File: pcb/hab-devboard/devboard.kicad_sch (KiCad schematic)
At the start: 90 parts, among them J1 S2B-PH-K-S, J2 SM04B-GHS-TB, J3 SM04B-GHS-TB, J4 2x20 Pin Header, J5 S2B-PH-K-S, Q1 DMG2301L, Q2 CSD25310Q2, Q3 BSS138, Q4 BSS138, Q5 BSS138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

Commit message: Updating pcb, adding xcode project for macOS gui
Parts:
- added H5: MountingHole, MountingHole:MountingHole_3.2mm_M3, symbol Mechanical:MountingHole
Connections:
- net 5VSNS is gone; now on net 5V_SNS: U8.1 (OUT)
- net +3V3_SBC: now also U5.4 (~{CS})
- net 5V_HEATER_EN: now also J4.18 (Pin_18)
- net 5V_PA_EN: now also J4.16 (Pin_16)
- net BATT_ALERT_N: now also J4.31 (Pin_31)
- net GPS_RST_N: now also J4.35 (Pin_35)
- net GPS_WAKE: now also J4.33 (Pin_33)
- net 5V_SNS: now reaches J4.37 (Pin_37)
- no-connect marks 41 -> 37
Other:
- note added: "CHECK THIS"
- note added: "External 5V Heater Power"
- note added: "Internal PU"
- moved on the sheet: J1, Q1, R1

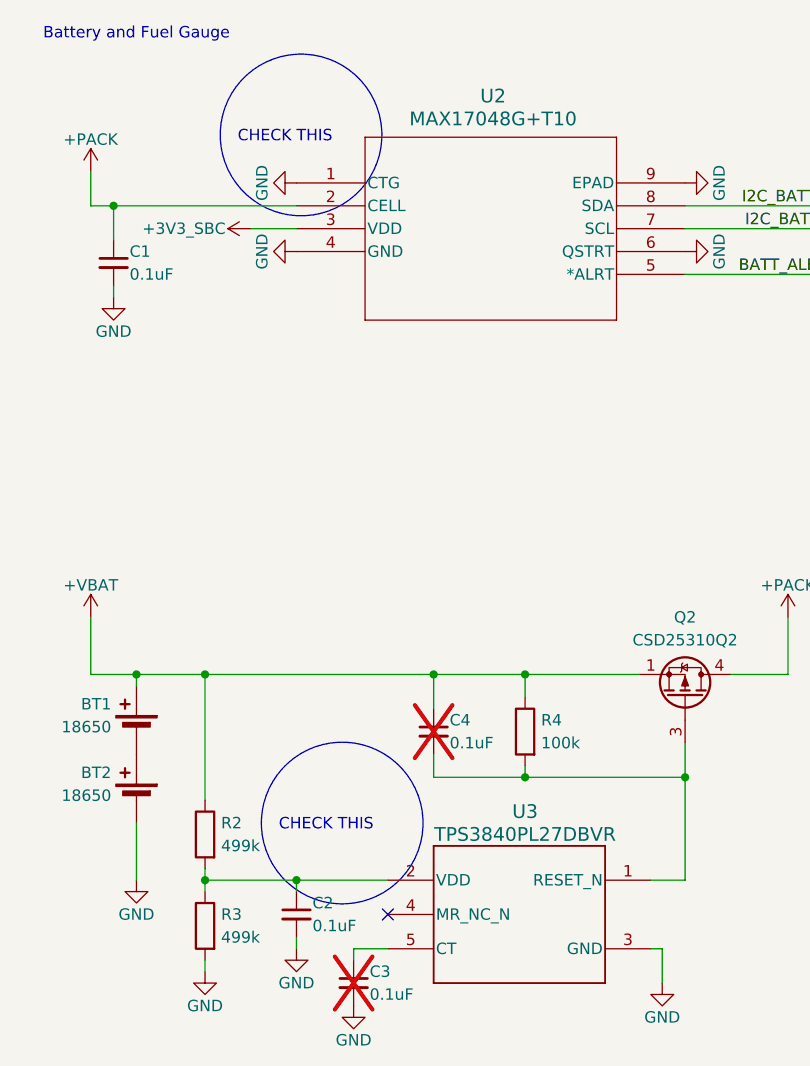
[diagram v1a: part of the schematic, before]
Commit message: major overhaul for rflink. Python scripts for gr-dvbs rx/tx. Tested in loopback mode. Have not added mpeg pipeline yet. See readme for details. Exported pcb files for fab
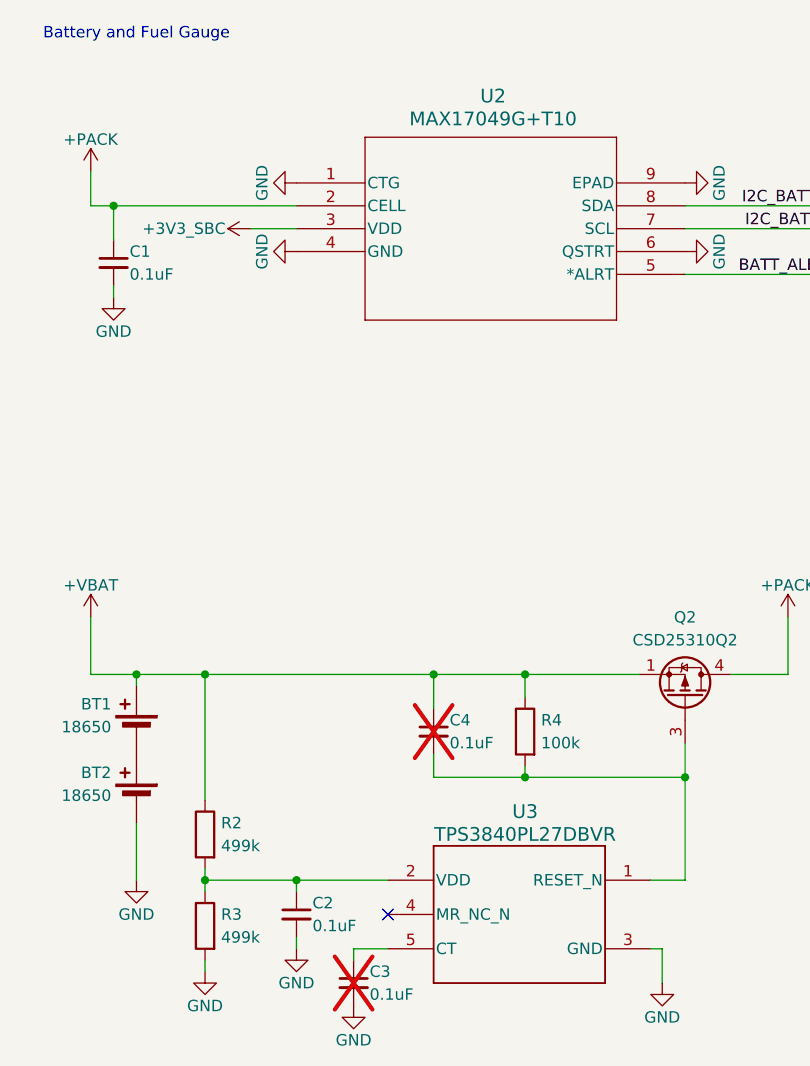
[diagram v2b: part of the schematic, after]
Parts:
- U2: value MAX17048G+T10 -> MAX17049G+T10
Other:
- note removed: "CHECK THIS"
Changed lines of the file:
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@@
 		(rev "A")
 	)
-	(circle
-		(center 48.26 102.87)
-		(radius 8.9803)
-		(stroke
-			(width 0)
-			(type default)
-		)
-		(fill
-			(type none)
-		)
-	)
-	(circle
-		(center 43.688 26.416)
-		(radius 8.9803)
-		(stroke
-			(width 0)
-			(type default)
-		)
-		(fill
-			(type none)
-		)
-	)
 	(text "Temp & Accel\nI2C0_M1"
 		(exclude_from_sim no)
@@
 		)
 	)
-	(text "CHECK THIS"
-		(exclude_from_sim no)
-		(at 46.482 103.124 0)
-		(effects
-			(font
-				(size 1.27 1.27)
-			)
-		)
-	)
 	(text "External 5V Heater Power"
 		(exclude_from_sim no)
@@
 		)
 	)
-	(text "CHECK THIS"
-		(exclude_from_sim no)
-		(at 41.91 26.67 0)
-		(effects
-			(font
-				(size 1.27 1.27)
-			)
-		)
-	)
 	(text "External 5V PA Power"
 		(exclude_from_sim no)
@@
 			)
 		)
-		(property "Value" "MAX17048G+T10"
+		(property "Value" "MAX17049G+T10"
 			(at 65.024 24.638 0)
 			(effects
